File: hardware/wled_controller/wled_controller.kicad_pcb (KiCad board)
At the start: 2 copper layers, 76 parts, among them J1 Screw_Terminal_01x03, J10 Screw_Terminal_01x03, J11 Screw_Terminal_01x03, J12 Screw_Terminal_01x03, J13 Screw_Terminal_01x03, J14 Screw_Terminal_01x03, J15 Screw_Terminal_01x03, J16 Screw_Terminal_01x02, J17 USB_B, J18 Header_01x05, J19 DIN-5_180degree, J2 Screw_Terminal_01x03, J20 DIN-5_180degree, J21 NC3MAH, J22 NC3FAH, J3 Screw_Terminal_01x03, J4 Screw_Terminal_01x03, J5 Screw_Terminal_01x03, J6 Screw_Terminal_01x03, J7 Screw_Terminal_01x03, J8 Screw_Terminal_01x03, J9 Screw_Terminal_01x03, U1 Pico, U10 TLV74333, U2 74HCT125, U3 74HCT125, U4 74HCT125, U5 LMR54410, U6 ADUM4160, U7 6N137, U8 74HCT125, U9 ISO35T

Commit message: some progress on PCB
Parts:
- removed the C13 at (156.5, 120.8)
- removed C3: 100nF, Capacitor_SMD:C_0805_2012Metric
- added D2: S2A, Diode_SMD:D_SMB, F.Cu at (185.0, -13.5)
- added F1: Fuse, conn:Fuseholder_FS002, F.Cu at (210.5, -15.5)
- added FID1: Fiducial, Fiducial:Fiducial_1mm_Mask2mm, F.Cu at (141.3, -118.7)
- added FID2: Fiducial, Fiducial:Fiducial_1mm_Mask2mm, F.Cu at (195.3, -44.8)
- added FID3: Fiducial, Fiducial:Fiducial_1mm_Mask2mm, F.Cu at (279.0, -16.0)
- added H1: MountingHole_Pad, mechanical:MountingHole_3.2mm_M3_DIN965_Pad, F.Cu at (115.5, -117.0)
- added H2: MountingHole_Pad, mechanical:MountingHole_3.2mm_M3_DIN965_Pad, F.Cu at (276.5, -6.50)
- added H3: MountingHole_Pad, mechanical:MountingHole_3.2mm_M3_DIN965_Pad, F.Cu at (115.5, -6.50)
- added H4: MountingHole_Pad, mechanical:MountingHole_3.2mm_M3_DIN965_Pad, F.Cu at (169.2, -43.8)
- added H5: MountingHole_Pad, mechanical:MountingHole_3.2mm_M3_DIN965_Pad, F.Cu at (151.0, -117.0)
- added H6: MountingHole_Pad, mechanical:MountingHole_3.2mm_M3_DIN965_Pad, F.Cu at (275.0, -44.1)
- J1, J10, J11, J12, J13, J14, J15, J2, J3, J4, J5, J6, J7, J8, J9: footprint conn:TerminalBlock_4Ucon_1x03_P3.50mm_Vertical -> conn:TerminalBlock_Degson_1x03_P3.50mm_Horizontal
- J16: footprint conn:TerminalBlock_4Ucon_1x02_P3.50mm_Vertical -> conn:TerminalBlock_1x02_P5.00mm_Horizontal
- J19, J20: footprint conn:57PC5F -> conn:DIN5_57PC5F
- R1, R10, R11, R12, R19, R2, R20, R21, R3, R4, R5, R6, R7, R8, R9: value 100Ω -> 100Ω
- U8: renamed from U7; footprint Package_DIP:DIP-8_W7.62mm -> Package_DIP:SMDIP-8_W9.53mm
- moved U6 220.1 mm to (146.6, -105.7), turned to 90 degrees
- moved J21 216.6 mm to (112.0, -93.2), turned to -90 degrees
- moved R14 215.6 mm to (147.0, -100.0), turned to 180 degrees
- moved C13 215.1 mm to (128.9, -89.5), turned to -90 degrees
- moved U10 214.2 mm to (117.5, -70.8), turned to 180 degrees
- moved L1 213.7 mm to (139.7, -104.8), turned to 180 degrees
- moved R13 213.4 mm to (142.9, -100.0), turned to 180 degrees
- moved R16 211.5 mm to (128.9, -79.7), turned to 90 degrees
- moved C16 210.5 mm to (122.6, -74.9)
- moved C6 209.4 mm to (144.1, -109.9)
- moved C17 207.2 mm to (117.2, -67.6)
- moved C7 206.6 mm to (133.0, -104.8), turned to 90 degrees
- moved C15 202.5 mm to (122.6, -69.8)
- moved C14 202.1 mm to (122.6, -72.4)
- moved C5 201.5 mm to (149.9, -105.7), turned to -90 degrees
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- renumbered C14 to C13, C15 to C14, C16 to C15, C17 to C16, C18 to C17, D2 to D3, D3 to D4, U8 to U5, U5 to U6, U6 to U7
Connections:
- C9 pad 2: GND -> Net-(J17-GND)
- J10 pad 2: /Drivers/WLED driver 10/DOUT -> /Drivers/WLED driver 12/DOUT
- J11 pad 2: /Drivers/WLED driver 11/DOUT -> /Drivers/WLED driver 5/DOUT
- J12 pad 2: /Drivers/WLED driver 12/DOUT -> /Drivers/WLED driver 15/DOUT
- J13 pad 2: /Drivers/WLED driver 13/DOUT -> /Drivers/WLED driver 6/DOUT
- J15 pad 2: /Drivers/WLED driver 15/DOUT -> /Drivers/WLED driver 13/DOUT
- J16 pad 1: VDD -> GND
- J16 pad 2: GND -> Net-(J16-Pin_2)
- J4 pad 2: /Drivers/WLED driver 4/DOUT -> /Drivers/WLED driver 7/DOUT
- J5 pad 2: /Drivers/WLED driver 5/DOUT -> /Drivers/WLED driver 10/DOUT
- J6 pad 2: /Drivers/WLED driver 6/DOUT -> /Drivers/WLED driver 9/DOUT
- J7 pad 2: /Drivers/WLED driver 7/DOUT -> /Drivers/WLED driver 8/DOUT
- J8 pad 2: /Drivers/WLED driver 8/DOUT -> /Drivers/WLED driver 11/DOUT
- J9 pad 2: /Drivers/WLED driver 9/DOUT -> /Drivers/WLED driver 4/DOUT
- R10 pad 1: Net-(U4D-O) -> Net-(U3B-O)
- R11 pad 1: Net-(U4A-O) -> Net-(U3A-O)
- R12 pad 1: Net-(U4B-O) -> Net-(U5D-O)
- R18 pad 1: Net-(U8D-O) -> Net-(U4B-O)
- R7 pad 1: Net-(U3A-O) -> Net-(U4C-O)
- R8 pad 1: Net-(U3B-O) -> Net-(U4D-O)
- R9 pad 1: Net-(U4C-O) -> Net-(U4A-O)
- U1 pad 1: unconnected-(U1-GPIO0-Pad1) -> /DMX512/RX
- U1 pad 2: /MIDI/MIDI_UART -> /DMX512/TX
- U1 pad 4: unconnected-(U1-GPIO2-Pad4) -> /DMX512/DIR
- U1 pad 5: /DMX512/DIR -> unconnected-(U1-GPIO3-Pad5)
- U1 pad 6: /DMX512/RX -> unconnected-(U1-GPIO4-Pad6)
- U1 pad 7: /DMX512/TX -> /MIDI/MIDI_UART
- U2 pad 12: /D8 -> /D7
- U2 pad 2: /D9 -> /D6
- U2 pad 5: /D11 -> /D5
- U2 pad 9: /D7 -> /D4
- U3 pad 12: /D12 -> /D11
- U3 pad 2: /D1 -> /D10
- U3 pad 5: /D2 -> /D9
- U3 pad 9: /D10 -> /D8
- U4 pad 12: /D4 -> /D2
- U4 pad 2: /D5 -> /D3
- U4 pad 4: /DEN -> +5V
- U4 pad 5: /D6 -> /MIDI/MIDI_UART
- U4 pad 9: /D3 -> /D1
- U5 pad 11: Net-(U8D-O) -> Net-(U5D-O)
- U5 pad 12: /MIDI/MIDI_UART -> /D13
- U5 pad 13: +5V -> /DEN
- U5 pad 2: /D13 -> /D15
- U5 pad 9: /D15 -> /D12
- U7 pad 10: Net-(J18-Pin_2) -> Net-(J18-Pin_3)
- U7 pad 11: Net-(J18-Pin_3) -> Net-(J18-Pin_2)
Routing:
- net VDD: track 0.00 -> 382.4 mm, vias 0 -> 3
- net +5V: track 0.00 -> 225.9 mm, vias 0 -> 6
- net Net-(U5A-O): track 0.00 -> 114.3 mm
- net Net-(U5B-O): track 0.00 -> 111.5 mm
- net Net-(U5D-O): track 0.00 -> 90.9 mm
- net /MIDI/MIDI_UART: track 0.00 -> 83.7 mm
- net Net-(U3A-O): track 0.00 -> 83.1 mm
- net Net-(U5C-O): track 0.00 -> 82.9 mm
- net /D1: track 0.00 -> 69.4 mm
- net Net-(U3D-O): track 0.00 -> 65.9 mm
- net /D2: track 0.00 -> 65.3 mm
- net Net-(U3B-O): track 0.00 -> 64.3 mm
- net /D15: track 0.00 -> 60.3 mm
- net /D13: track 0.00 -> 58.2 mm, vias 0 -> 2
- net /D4: track 0.00 -> 56.4 mm
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- added copper zone on B.Cu, net Net-(J17-GND)
- added copper zone on F.Cu, net Net-(J17-GND)
- added copper zone on B.Cu, net Net-(U10-GND)
- added copper zone on F.Cu, net Net-(U10-GND)
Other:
- board outline added: 188 x 128 mm

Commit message: work on pcb
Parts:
- removed the C12 at (112.2, 127.6)
- removed the H4 at (169.2, -43.8)
- removed H6: MountingHole_Pad, mechanical:MountingHole_3.2mm_M3_DIN965_Pad
- added R15: 10kΩ, Resistor_SMD:R_0805_2012Metric, F.Cu at (128.9, -83.5)
- moved C10 149.0 mm to (168.0, -13.7), turned to 90 degrees
- moved FID2 81.9 mm to (113.3, -45.4)
- moved C5 6.04 mm to (144.5, -103.8), turned to 90 degrees
- moved C4 1.59 mm to (151.4, -105.7)
- moved U6 1.08 mm to (147.6, -105.7)
- renumbered C11 to C10, C13 to C11, C14 to C12, C15 to C13, C16 to C14, C17 to C15, C4 to C3, C5 to C4, C6 to C5, C7 to C6, C8 to C7, C9 to C8, C10 to C9, H5 to H4, R15 to R16, R16 to R17, R17 to R18, R18 to R19, R19 to R20, R20 to R21, R21 to R22
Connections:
- U1 pad 10: /D2 -> /D9
- U1 pad 11: /D3 -> /D8
- U1 pad 12: /D4 -> /D6
- U1 pad 14: /D5 -> /D7
- U1 pad 15: /D6 -> /D5
- U1 pad 16: /D7 -> /D4
- U1 pad 17: /D8 -> /D3
- U1 pad 19: /D9 -> /D2
- U1 pad 20: /D10 -> /D1
- U1 pad 21: /D11 -> /D15
- U1 pad 22: /D12 -> /D14
- U1 pad 24: /D13 -> /D12
- U1 pad 25: /D14 -> /D13
- U1 pad 26: /D15 -> /D10
- U1 pad 9: /D1 -> /D11
- U6 pad 1: GND -> Net-(U6-CB)
- U6 pad 2: (no net) -> GND
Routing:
- net /DEN: track 0.00 -> 155.8 mm, vias 0 -> 11
- net /USB_EN: track 0.00 -> 69.4 mm, vias 0 -> 3
- net /D1: track 69.4 -> 41.0 mm
- net /D11: track 44.0 -> 71.0 mm
- net /D9: track 34.6 -> 60.4 mm
- net GND: track 0.00 -> 24.5 mm, vias 1 -> 24
- net /D2: track 65.3 -> 42.6 mm
- net /D10: track 32.3 -> 54.4 mm
- net /D8: track 46.4 -> 64.8 mm
- net /D3: track 54.7 -> 40.0 mm
- net /D15: track 60.3 -> 47.1 mm
- net /D12: track 51.2 -> 59.3 mm
- net /D6: track 44.2 -> 52.2 mm
- net /D7: track 47.8 -> 55.6 mm
- net /D4: track 56.4 -> 48.9 mm
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- added copper zone on B.Cu, net GND
- added copper zone on F.Cu, net GND
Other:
- outline, holes or cut-outs redrawn

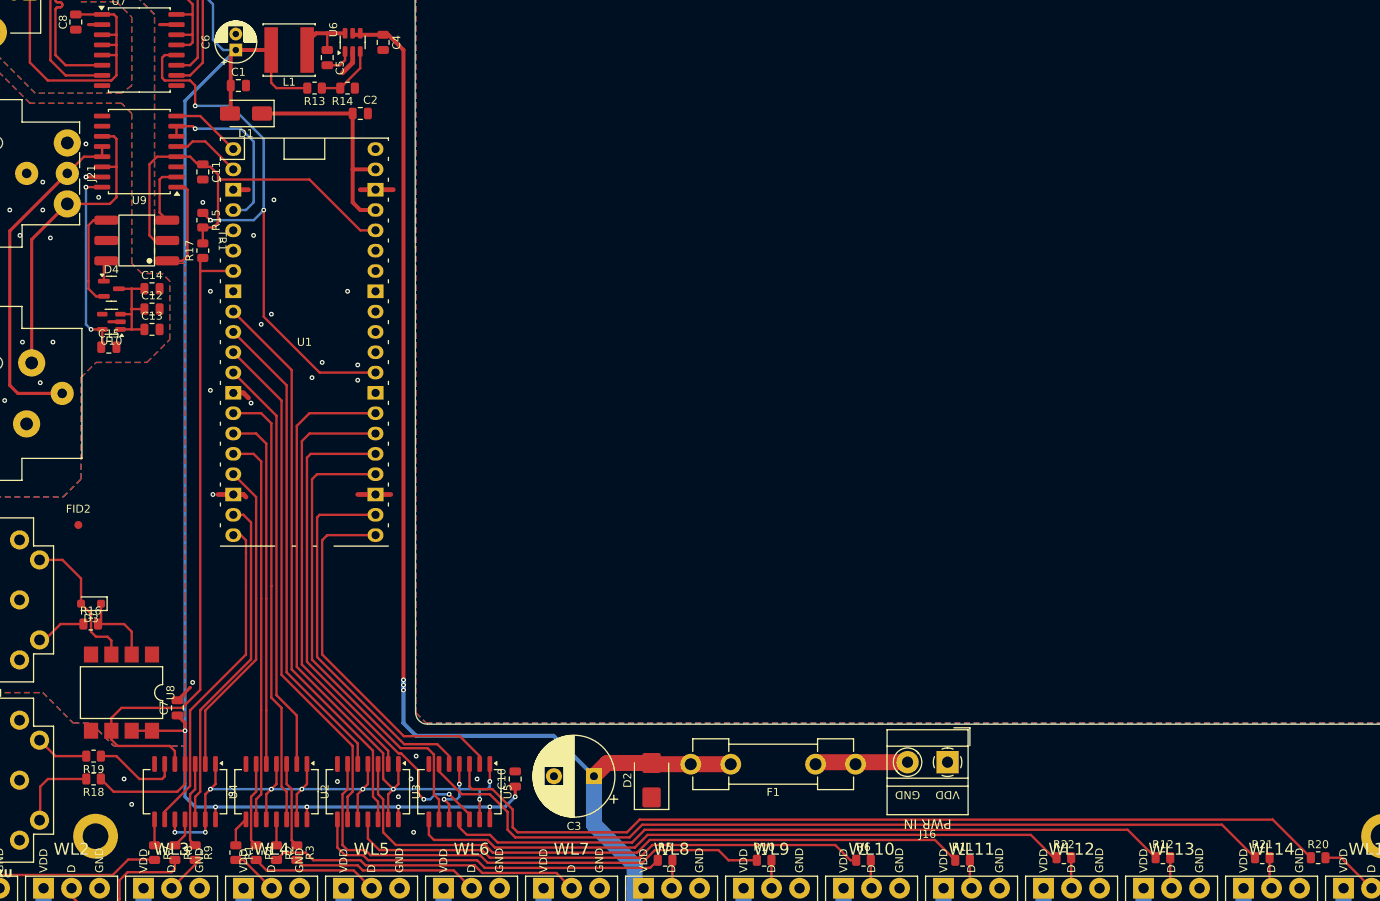
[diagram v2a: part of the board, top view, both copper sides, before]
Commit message: dmx512 line TVS
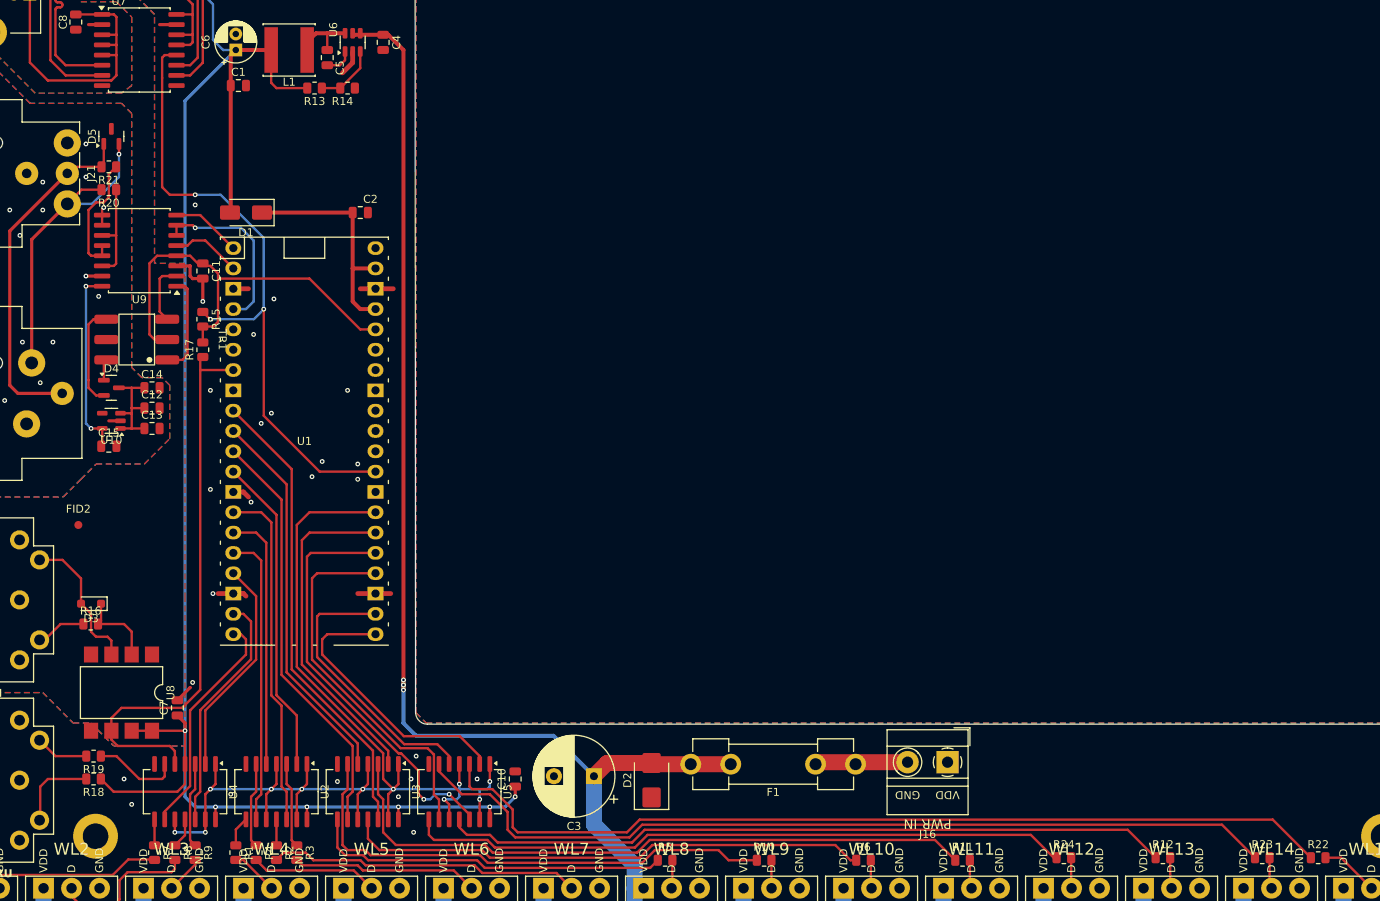
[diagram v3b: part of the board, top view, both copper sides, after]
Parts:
- added D5: SM712, Package_TO_SOT_SMD:SOT-23, F.Cu at (117.5, -94.0)
- added R20: 10Ω, Resistor_SMD:R_0805_2012Metric, F.Cu at (117.2, -87.3)
- added R21: 10Ω, Resistor_SMD:R_0805_2012Metric, F.Cu at (117.2, -90.2)
- moved C14 12.4 mm to (122.6, -62.5)
- moved C2 12.4 mm to (148.6, -84.5)
- moved D1 12.4 mm to (134.3, -84.5)
- moved D4 12.4 mm to (117.5, -62.5)
- moved TR1 12.4 mm to (124.5, -68.6)
- moved U9 12.4 mm to (121.0, -79.7)
- moved C12 12.4 mm to (122.6, -60.0)
- moved C15 12.4 mm to (117.2, -55.2)
- moved U1 12.4 mm to (141.6, -55.9)
- moved C11 12.4 mm to (128.9, -77.2)
- moved C13 12.4 mm to (122.6, -57.5)
- moved R15 12.4 mm to (128.9, -71.1)
- moved R17 12.4 mm to (128.9, -67.3)
- moved U10 12.4 mm to (117.5, -58.4)
- renumbered R20 to R22, R21 to R23, R22 to R24
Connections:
- J21 pad 2: Net-(U9-A) -> Net-(D5-K-Pad2)
- J21 pad 3: Net-(U9-B) -> Net-(D5-K-Pad1)
- J22 pad 2: Net-(U9-A) -> Net-(D5-K-Pad2)
- J22 pad 3: Net-(U9-B) -> Net-(D5-K-Pad1)
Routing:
- net Net-(D5-K-Pad1): track 0.00 -> 44.0 mm
- net Net-(D5-K-Pad2): track 0.00 -> 38.7 mm, vias 0 -> 1
- net Net-(U9-B): track 42.9 -> 15.9 mm
- net Net-(U9-A): track 39.2 -> 12.9 mm
- net +5V: track 230.8 -> 243.2 mm
- net /MIDI/MIDI_UART: track 83.7 -> 71.3 mm
- net /D8: track 64.8 -> 52.5 mm
- net /D15: track 47.1 -> 34.8 mm
- net /D10: track 54.4 -> 42.0 mm
- net /D9: track 60.4 -> 48.1 mm
- net /D7: track 55.6 -> 43.2 mm
- net /D6: track 52.2 -> 39.8 mm
- net /D4: track 48.9 -> 36.5 mm
- net /D14: track 47.5 -> 35.1 mm
- net /D13: track 65.3 -> 53.0 mm
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
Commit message: final pcb touches
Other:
- board text added: "Milena's lamp board v0.1"
